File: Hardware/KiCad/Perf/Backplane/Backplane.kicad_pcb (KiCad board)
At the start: 2 copper layers, 9 parts, among them P1 CONN_02X20, P2 CONN_02X20, P3 CONN_02X16, P4 CONN_02X16, P5 CONN_02X16, P6 CONN_02X16, P7 CONN_02X16, P8 CONN_02X16, P9 CONN_02X16

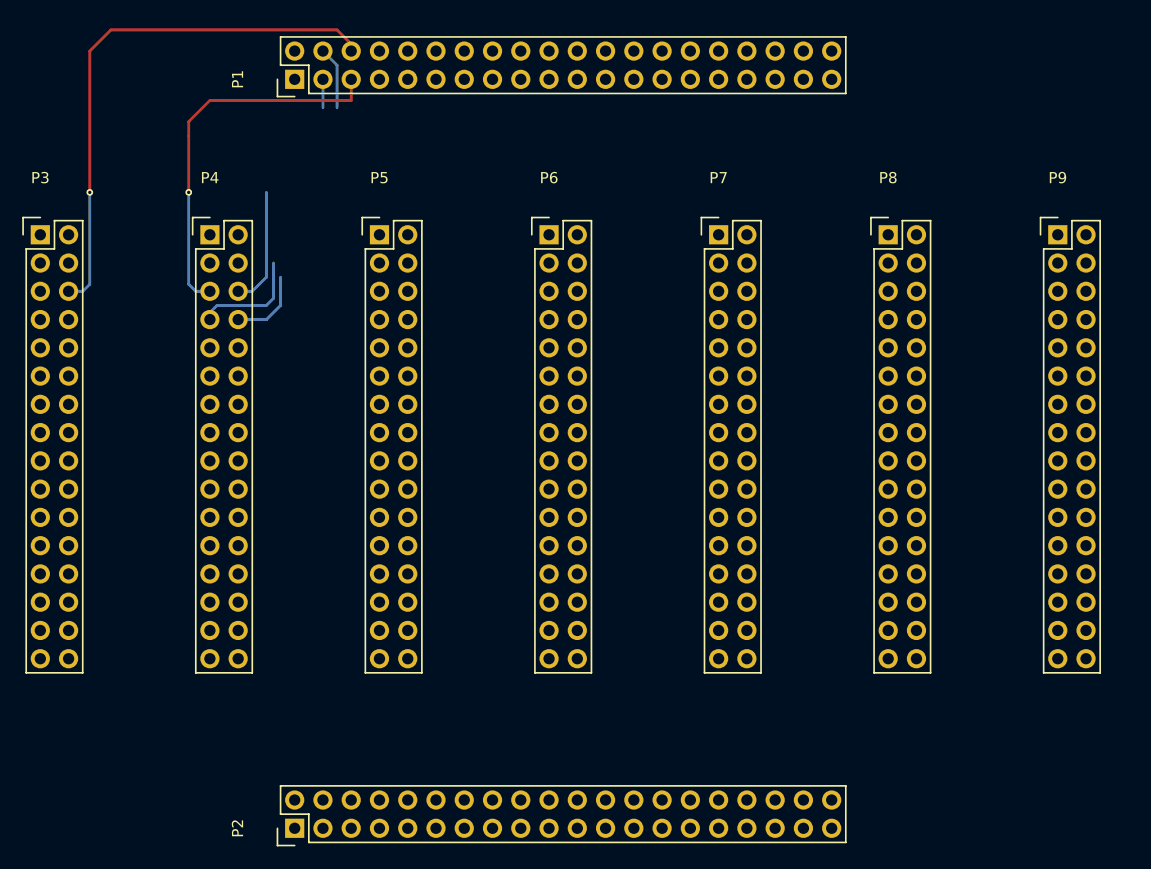
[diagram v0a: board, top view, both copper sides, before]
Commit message: laying out motherboard and backplane
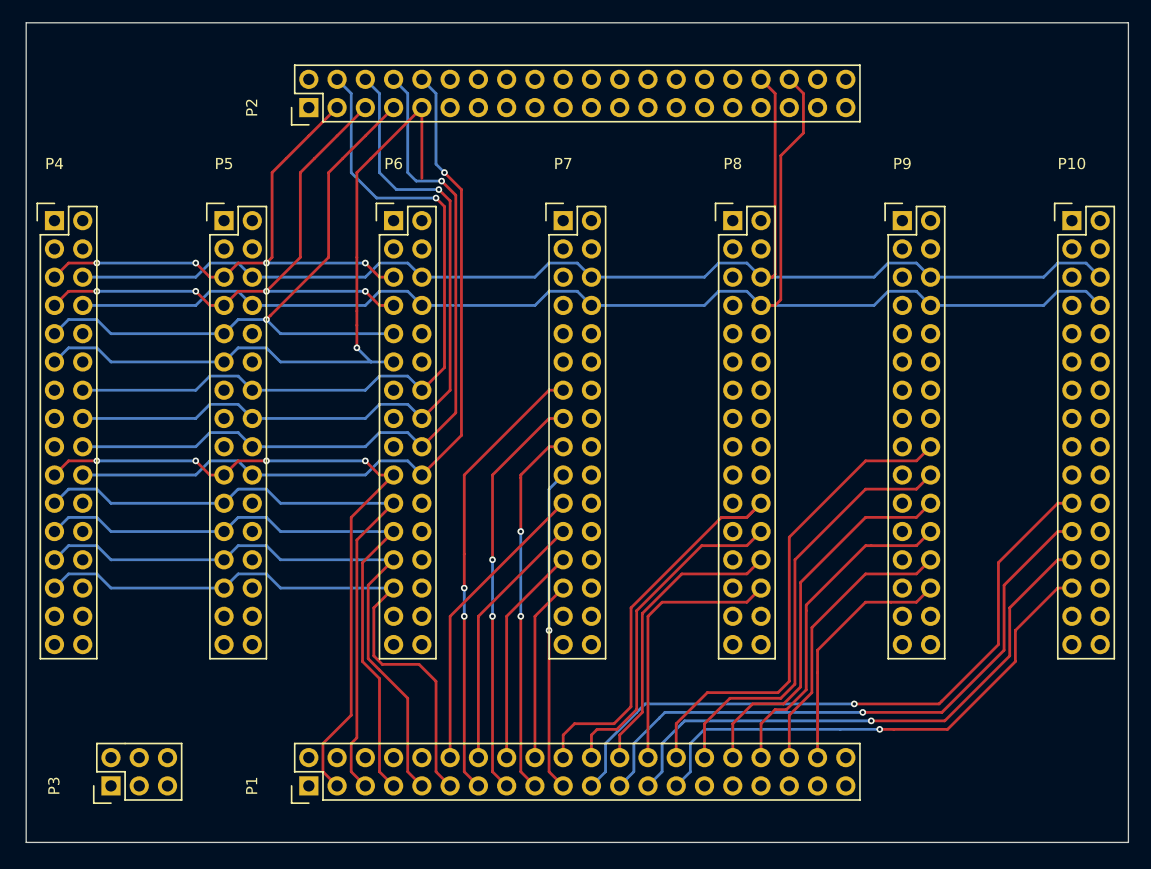
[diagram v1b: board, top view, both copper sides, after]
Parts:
- added P10: POWER, Pin_Headers:Pin_Header_Straight_2x16, F.Cu at (134.6, 71.1)
- P3: value CONN_02X16 -> CONN_02X03; footprint Pin_Headers:Pin_Header_Straight_2x16 -> Pin_Headers:Pin_Header_Straight_2x03
- P4: value CONN_02X16 -> AUX 3
- P5: value CONN_02X16 -> AUX 2
- P6: value CONN_02X16 -> AUX 1
- P7: value CONN_02X16 -> COMMUNICATION
- P8: value CONN_02X16 -> LIGHT
- P9: value CONN_02X16 -> MANIPULTOR
- moved P2 64.8 mm to (66.0, 61.0)
- moved P1 63.5 mm to (66.0, 121.9)
- moved P3 49.9 mm to (48.3, 121.9), turned to 90 degrees
- moved P4 14.0 mm to (43.2, 71.1)
- moved P5 14.0 mm to (58.4, 71.1)
- moved P6 14.0 mm to (73.7, 71.1)
- moved P7 14.0 mm to (88.9, 71.1)
- moved P8 14.0 mm to (104.1, 71.1)
- moved P9 14.0 mm to (119.4, 71.1)
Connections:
- P1 pad 11: Net-(P1-Pad11) -> GPIO_15
- P1 pad 12: Net-(P1-Pad12) -> SPI_1_NSS
- P1 pad 13: Net-(P1-Pad13) -> USART_3_TX
- P1 pad 14: Net-(P1-Pad14) -> SPI_1_SCK
- P1 pad 15: Net-(P1-Pad15) -> USART_3_RX
- P1 pad 16: Net-(P1-Pad16) -> SPI_1_MSIO
- P1 pad 17: Net-(P1-Pad17) -> USART_3_CK
- P1 pad 18: Net-(P1-Pad18) -> SPI_1_MOSI
- P1 pad 19: Net-(P1-Pad19) -> USART_3_CTS
- P1 pad 20: Net-(P1-Pad20) -> TIM_2_CH_1
- P1 pad 21: Net-(P1-Pad21) -> ADC_10
- P1 pad 22: Net-(P1-Pad22) -> TIM_2_CH_2
- P1 pad 23: Net-(P1-Pad23) -> ADC_11
- P1 pad 24: Net-(P1-Pad24) -> TIM_2_CH_3
- P1 pad 25: Net-(P1-Pad25) -> ADC_12
- P1 pad 26: Net-(P1-Pad26) -> TIM_2_CH_4
- P1 pad 27: Net-(P1-Pad27) -> ADC_13
- P1 pad 28: Net-(P1-Pad28) -> TIM_13
- P1 pad 3: Net-(P1-Pad3) -> GPIO_11
- P1 pad 30: Net-(P1-Pad30) -> TIM_14
- P1 pad 32: Net-(P1-Pad32) -> TIM_12_CH_1
- P1 pad 34: Net-(P1-Pad34) -> TIM_12_CH_2
- P1 pad 36: Net-(P1-Pad36) -> TIM_15_CH_1
- P1 pad 38: Net-(P1-Pad38) -> TIM_15_CH_2
- P1 pad 4: Net-(P1-Pad4) -> I2C_2_SCL
- P1 pad 5: +3V3 -> GPIO_12
- P1 pad 6: +5V -> I2C_2_SDA
- P1 pad 7: Net-(P1-Pad7) -> GPIO_13
- P1 pad 9: Net-(P1-Pad9) -> GPIO_14
- P2 pad 10: Net-(P2-Pad10) -> GPIO_24
- P2 pad 11: Net-(P2-Pad11) -> GPIO_27
- P2 pad 12: Net-(P2-Pad12) -> GPIO_20
- P2 pad 13: Net-(P2-Pad13) -> GPIO_26
- P2 pad 14: Net-(P2-Pad14) -> GPIO_19
- P2 pad 15: Net-(P2-Pad15) -> GPIO_25
- P2 pad 16: Net-(P2-Pad16) -> GPIO_18
- P2 pad 17: Net-(P2-Pad17) -> USART_2_CK
- P2 pad 18: Net-(P2-Pad18) -> GPIO_17
- P2 pad 19: Net-(P2-Pad19) -> USART_2_RX
- P2 pad 20: Net-(P2-Pad20) -> GPIO_16
- P2 pad 21: Net-(P2-Pad21) -> USART_2_TX
- P2 pad 22: Net-(P2-Pad22) -> GPIO_0
- P2 pad 23: Net-(P2-Pad23) -> UART_5_RX
- P2 pad 24: Net-(P2-Pad24) -> GPIO_1
- P2 pad 25: Net-(P2-Pad25) -> UART_5_TX
- P2 pad 26: Net-(P2-Pad26) -> GPIO_2
- P2 pad 27: Net-(P2-Pad27) -> UART_4_RX
- P2 pad 28: Net-(P2-Pad28) -> GPIO_3
- P2 pad 29: Net-(P2-Pad29) -> UART_4_TX
- P2 pad 3: Net-(P2-Pad3) -> GPIO_31
- P2 pad 30: Net-(P2-Pad30) -> GPIO_4
- P2 pad 31: Net-(P2-Pad31) -> GPIO_7
- P2 pad 32: Net-(P2-Pad32) -> GPIO_5
- P2 pad 33: Net-(P2-Pad33) -> GPIO_8
- P2 pad 34: Net-(P2-Pad34) -> I2C_2_SCL
- P2 pad 35: Net-(P2-Pad35) -> GPIO_9
- P2 pad 36: Net-(P2-Pad36) -> I2C_2_SDA
- P2 pad 37: Net-(P2-Pad37) -> GPIO_10
- P2 pad 4: Net-(P2-Pad4) -> GPIO_21
- P2 pad 5: +3V3 -> GPIO_30
- P2 pad 6: +5V -> GPIO_22
- P2 pad 7: Net-(P2-Pad7) -> GPIO_29
- P2 pad 8: Net-(P2-Pad8) -> GPIO_23
- P2 pad 9: Net-(P2-Pad9) -> GPIO_28
- P3 pad 1: GND -> +3V3
- P3 pad 2: GND -> +5V
- P3 pad 3: Net-(P3-Pad3) -> +3V3
- P3 pad 4: Net-(P3-Pad4) -> +5V
- P3 pad 5: +3V3 -> GND
- P3 pad 6: +5V -> GND
- P4 pad 11: Net-(P4-Pad11) -> GPIO_28
- P4 pad 14: Net-(P4-Pad14) -> GPIO_21
- P4 pad 16: Net-(P4-Pad16) -> GPIO_22
- P4 pad 18: Net-(P4-Pad18) -> GPIO_23
- P4 pad 19: Net-(P4-Pad19) -> GPIO_11
- P4 pad 20: Net-(P4-Pad20) -> GPIO_24
- P4 pad 21: Net-(P4-Pad21) -> GPIO_12
- P4 pad 23: Net-(P4-Pad23) -> GPIO_13
- P4 pad 25: Net-(P4-Pad25) -> GPIO_14
- P4 pad 27: Net-(P4-Pad27) -> GPIO_15
- P4 pad 3: Net-(P4-Pad3) -> +3V3
- P4 pad 4: Net-(P4-Pad4) -> +5V
- P4 pad 5: +3V3 -> GPIO_31
- P4 pad 6: +5V -> I2C_2_SCL
- P4 pad 7: Net-(P4-Pad7) -> GPIO_30
- P4 pad 8: Net-(P4-Pad8) -> I2C_2_SDA
- P4 pad 9: Net-(P4-Pad9) -> GPIO_29
- P5 pad 11: Net-(P5-Pad11) -> GPIO_28
- P5 pad 14: Net-(P5-Pad14) -> GPIO_21
- P5 pad 16: Net-(P5-Pad16) -> GPIO_22
- P5 pad 18: Net-(P5-Pad18) -> GPIO_23
- P5 pad 19: Net-(P5-Pad19) -> GPIO_11
- P5 pad 20: Net-(P5-Pad20) -> GPIO_24
- P5 pad 21: Net-(P5-Pad21) -> GPIO_12
- P5 pad 23: Net-(P5-Pad23) -> GPIO_13
- P5 pad 25: Net-(P5-Pad25) -> GPIO_14
- P5 pad 27: Net-(P5-Pad27) -> GPIO_15
- P5 pad 3: Net-(P5-Pad3) -> +3V3
- P5 pad 4: Net-(P5-Pad4) -> +5V
- P5 pad 5: +3V3 -> GPIO_31
- P5 pad 6: +5V -> I2C_2_SCL
- P5 pad 7: Net-(P5-Pad7) -> GPIO_30
- P5 pad 8: Net-(P5-Pad8) -> I2C_2_SDA
- P5 pad 9: Net-(P5-Pad9) -> GPIO_29
- P6 pad 11: Net-(P6-Pad11) -> GPIO_28
- P6 pad 14: Net-(P6-Pad14) -> GPIO_21
- P6 pad 16: Net-(P6-Pad16) -> GPIO_22
- P6 pad 18: Net-(P6-Pad18) -> GPIO_23
- P6 pad 19: Net-(P6-Pad19) -> GPIO_11
- P6 pad 20: Net-(P6-Pad20) -> GPIO_24
- P6 pad 21: Net-(P6-Pad21) -> GPIO_12
- P6 pad 23: Net-(P6-Pad23) -> GPIO_13
- P6 pad 25: Net-(P6-Pad25) -> GPIO_14
- P6 pad 27: Net-(P6-Pad27) -> GPIO_15
- P6 pad 3: Net-(P6-Pad3) -> +3V3
- P6 pad 4: Net-(P6-Pad4) -> +5V
- P6 pad 5: +3V3 -> GPIO_31
- P6 pad 6: +5V -> I2C_2_SCL
- P6 pad 7: Net-(P6-Pad7) -> GPIO_30
- P6 pad 8: Net-(P6-Pad8) -> I2C_2_SDA
- P6 pad 9: Net-(P6-Pad9) -> GPIO_29
- P7 pad 10: Net-(P7-Pad10) -> USART_2_CK
- P7 pad 12: Net-(P7-Pad12) -> USART_2_RX
- P7 pad 13: Net-(P7-Pad13) -> USART_3_TX
- P7 pad 14: Net-(P7-Pad14) -> USART_2_TX
- P7 pad 15: Net-(P7-Pad15) -> USART_3_RX
- P7 pad 16: Net-(P7-Pad16) -> UART_5_RX
- P7 pad 17: Net-(P7-Pad17) -> USART_3_CK
- P7 pad 18: Net-(P7-Pad18) -> UART_5_TX
- P7 pad 19: Net-(P7-Pad19) -> USART_3_CTS
- P7 pad 20: Net-(P7-Pad20) -> UART_4_RX
- P7 pad 21: Net-(P7-Pad21) -> SPI_1_NSS
- P7 pad 22: Net-(P7-Pad22) -> UART_4_TX
- P7 pad 23: Net-(P7-Pad23) -> SPI_1_SCK
- P7 pad 25: Net-(P7-Pad25) -> SPI_1_MSIO
- P7 pad 27: Net-(P7-Pad27) -> SPI_1_MOSI
- P7 pad 3: Net-(P7-Pad3) -> +3V3
- P7 pad 4: Net-(P7-Pad4) -> +5V
- P7 pad 5: +3V3 -> GPIO_27
- P7 pad 6: +5V -> I2C_2_SCL
- P7 pad 7: Net-(P7-Pad7) -> GPIO_26
- P7 pad 8: Net-(P7-Pad8) -> I2C_2_SDA
- P7 pad 9: Net-(P7-Pad9) -> GPIO_25
- P8 pad 12: Net-(P8-Pad12) -> GPIO_20
- P8 pad 14: Net-(P8-Pad14) -> GPIO_19
- P8 pad 16: Net-(P8-Pad16) -> GPIO_18
- P8 pad 18: Net-(P8-Pad18) -> GPIO_17
- P8 pad 20: Net-(P8-Pad20) -> GPIO_16
- P8 pad 22: Net-(P8-Pad22) -> TIM_2_CH_1
- P8 pad 24: Net-(P8-Pad24) -> TIM_2_CH_2
- P8 pad 26: Net-(P8-Pad26) -> TIM_2_CH_3
- P8 pad 28: Net-(P8-Pad28) -> TIM_2_CH_4
- P8 pad 3: Net-(P8-Pad3) -> +3V3
- P8 pad 4: Net-(P8-Pad4) -> +5V
- P8 pad 5: +3V3 -> Net-(P8-Pad5)
- P8 pad 6: +5V -> I2C_2_SCL
- P8 pad 8: Net-(P8-Pad8) -> I2C_2_SDA
- P9 pad 11: Net-(P9-Pad11) -> GPIO_3
- P9 pad 13: Net-(P9-Pad13) -> GPIO_4
- P9 pad 15: Net-(P9-Pad15) -> GPIO_5
- P9 pad 18: Net-(P9-Pad18) -> TIM_13
- P9 pad 20: Net-(P9-Pad20) -> TIM_14
- P9 pad 22: Net-(P9-Pad22) -> TIM_12_CH_1
- P9 pad 24: Net-(P9-Pad24) -> TIM_12_CH_2
- P9 pad 26: Net-(P9-Pad26) -> TIM_15_CH_1
- P9 pad 28: Net-(P9-Pad28) -> TIM_15_CH_2
- P9 pad 3: Net-(P9-Pad3) -> +3V3
- P9 pad 4: Net-(P9-Pad4) -> +5V
- P9 pad 5: +3V3 -> GPIO_0
- P9 pad 6: +5V -> I2C_2_SCL
- P9 pad 7: Net-(P9-Pad7) -> GPIO_1
- P9 pad 8: Net-(P9-Pad8) -> I2C_2_SDA
- P9 pad 9: Net-(P9-Pad9) -> GPIO_2
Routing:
- net I2C_2_SDA: track 0.00 -> 120.9 mm
- net I2C_2_SCL: track 0.00 -> 117.2 mm
- net GPIO_24: track 0.00 -> 71.1 mm, vias 0 -> 1
- net GPIO_23: track 0.00 -> 70.5 mm, vias 0 -> 1
- net GPIO_22: track 0.00 -> 69.5 mm, vias 0 -> 1
- net GPIO_21: track 0.00 -> 68.5 mm, vias 0 -> 1
- net GPIO_28: track 0.00 -> 64.7 mm, vias 0 -> 1
- net GPIO_11: track 0.00 -> 63.7 mm, vias 0 -> 4
- net GPIO_12: track 0.00 -> 60.1 mm
- net ADC_10: track 0.00 -> 59.5 mm, vias 0 -> 1
- net +5V: track 59.3 -> 0.00 mm, vias 1 -> 0
- net GPIO_13: track 0.00 -> 57.8 mm
- net GPIO_29: track 0.00 -> 56.6 mm, vias 0 -> 1
- net GPIO_15: track 0.00 -> 55.9 mm
- net GPIO_14: track 0.00 -> 55.9 mm
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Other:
- board outline added: 99.1 x 73.7 mm

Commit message: updated footprints and some layout
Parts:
- moved P3 7.62 mm to (55.9, 121.9)

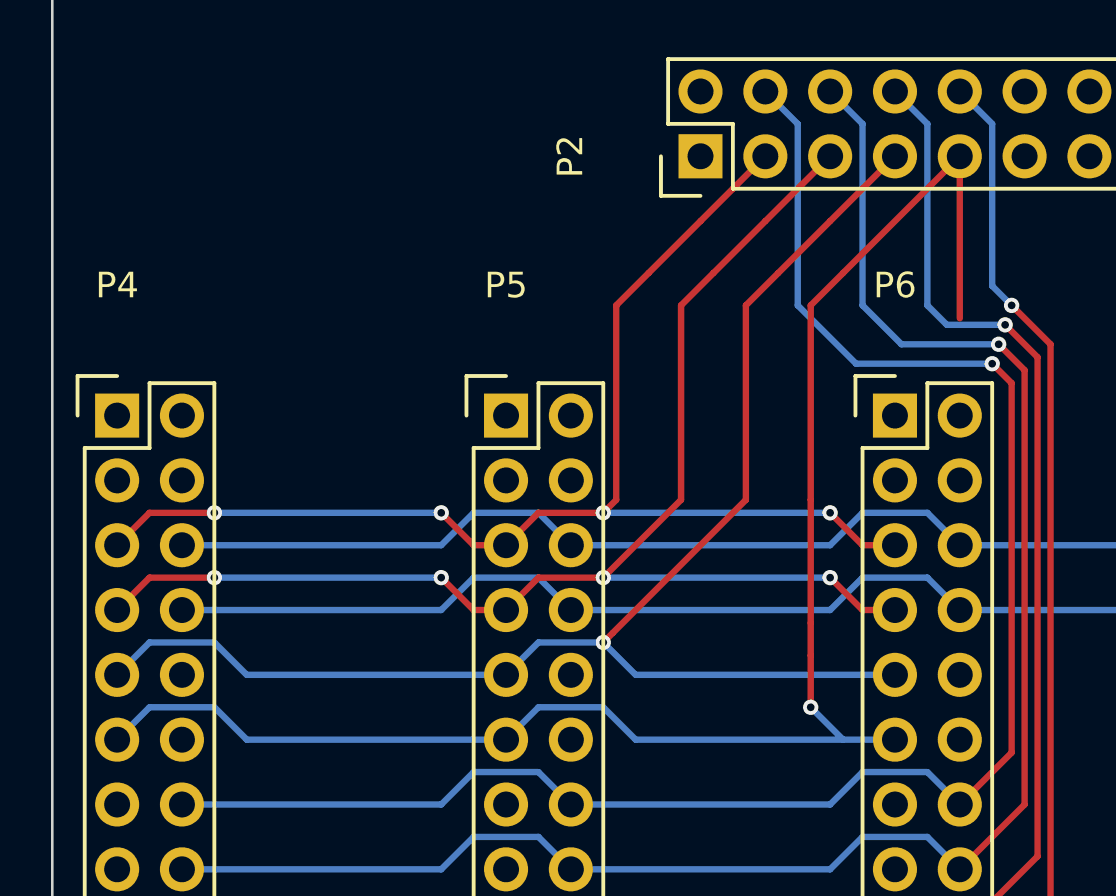
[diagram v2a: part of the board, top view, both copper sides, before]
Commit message: Small change to USART 2 pin layout from MB to Backplane
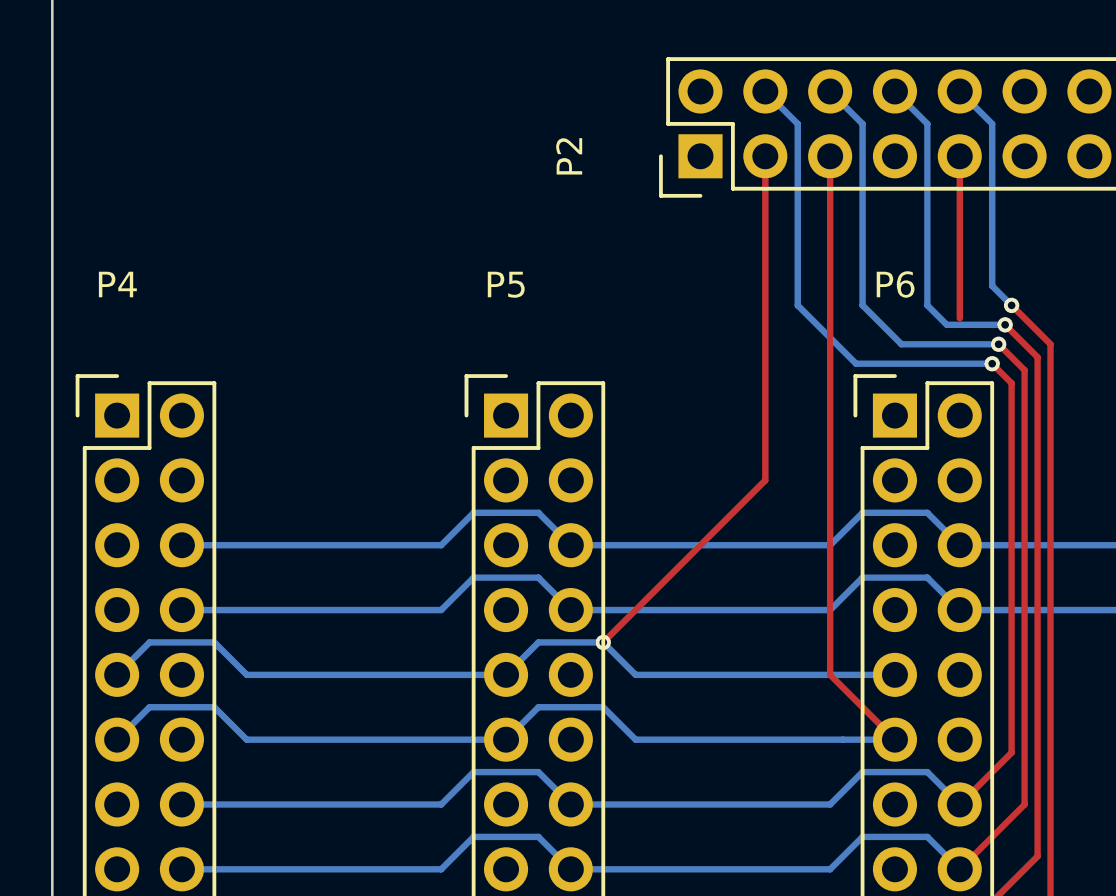
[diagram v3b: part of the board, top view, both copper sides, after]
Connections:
- P1 pad 10: Net-(P1-Pad10) -> I2C_2_SDA
- P1 pad 4: I2C_2_SCL -> Net-(P1-Pad4)
- P1 pad 6: I2C_2_SDA -> Net-(P1-Pad6)
- P1 pad 8: Net-(P1-Pad8) -> I2C_2_SCL
- P2 pad 11: GPIO_27 -> GPIO_25
- P2 pad 13: GPIO_26 -> USART_2_CK
- P2 pad 15: GPIO_25 -> USART_2_RX
- P2 pad 17: USART_2_CK -> USART_2_TX
- P2 pad 19: USART_2_RX -> USART_2_RTS
- P2 pad 21: USART_2_TX -> USART_2_CTS
- P2 pad 3: GPIO_31 -> GPIO_29
- P2 pad 5: GPIO_30 -> GPIO_28
- P2 pad 7: GPIO_29 -> GPIO_27
- P2 pad 9: GPIO_28 -> GPIO_26
- P4 pad 5: GPIO_31 -> Net-(P4-Pad5)
- P4 pad 7: GPIO_30 -> Net-(P4-Pad7)
- P5 pad 5: GPIO_31 -> Net-(P5-Pad5)
- P5 pad 7: GPIO_30 -> Net-(P5-Pad7)
- P6 pad 5: GPIO_31 -> Net-(P6-Pad5)
- P6 pad 7: GPIO_30 -> Net-(P6-Pad7)
- P7 pad 16: UART_5_RX -> USART_2_RTS
- P7 pad 18: UART_5_TX -> USART_2_CTS
- P7 pad 20: UART_4_RX -> UART_5_RX
- P7 pad 22: UART_4_TX -> UART_5_TX
- P7 pad 24: Net-(P7-Pad24) -> UART_4_RX
- P7 pad 26: Net-(P7-Pad26) -> UART_4_TX
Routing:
- net GPIO_30: track 54.0 -> 0.00 mm, vias 4 -> 0
- net GPIO_31: track 49.2 -> 0.00 mm, vias 4 -> 0
- net GPIO_28: track 64.7 -> 56.5 mm, vias 1 -> 0
- net GPIO_26: track 0.00 -> 6.35 mm
- net GPIO_29: track 56.6 -> 54.5 mm
- net Net-(P4-Pad7): track 0.00 -> 1.27 mm
